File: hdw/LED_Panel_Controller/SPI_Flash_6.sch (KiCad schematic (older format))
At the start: 0 parts

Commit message: more schematic development
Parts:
- added C? (x2): 0.1uF, Capacitors_SMD:C_0603, symbol Custom_Library:C_Custom
- added D?: Green, LEDs:LED_0603, symbol Device:LED
- added R? (x4): 10k, Resistors_SMD:R_0603, symbol Custom_Library:R_Custom
- added R? (x4): 10, symbol Custom_Library:R_Custom
- added R?: 1k, Resistors_SMD:R_0603, symbol Custom_Library:R_Custom
- added U?: SST25VF080B-50-4I-S2AF, Package_SO:SOIC-8_5.275x5.275mm_P1.27mm, symbol Memory_Flash:SST25VF080B-50-4x-S2Ax
- added U?: 74LVC1G97, Package_TO_SOT_SMD:SOT-363_SC-70-6, symbol Custom_Library:74LVC1G97_Power_BUF
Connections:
- new net: R?.1, R?.1, U?.2 (SO)
- new net: R?.1, R?.1, U?.5 (SI)
- new net: D?.1 (K), U?.4
- new net: D?.2 (A), R?.2
- new net: R?.1, R?.2, U?.1 (~CE)
- new net: R?.1, R?.1, U?.6 (SCK)
- new net +3V3: C?.1, C?.1, R?.1, R?.1, U?.3 (~WP~), U?.5 (VCC), U?.7 (~HOLD~), U?.8 (VDD)
- new net FLASH_SPI_MISO: R?.2
- new net FLASH_SPI_MOSI: R?.2
- new net FLASH_SPI_SCK: R?.2
- new net GND: C?.2, C?.2, R?.2, R?.2, R?.2, U?.2 (GND), U?.3 (GND), U?.4 (VSS), U?.6 (GND)
- new net ~FLASH_SPI_CE6: R?.2, U?.1

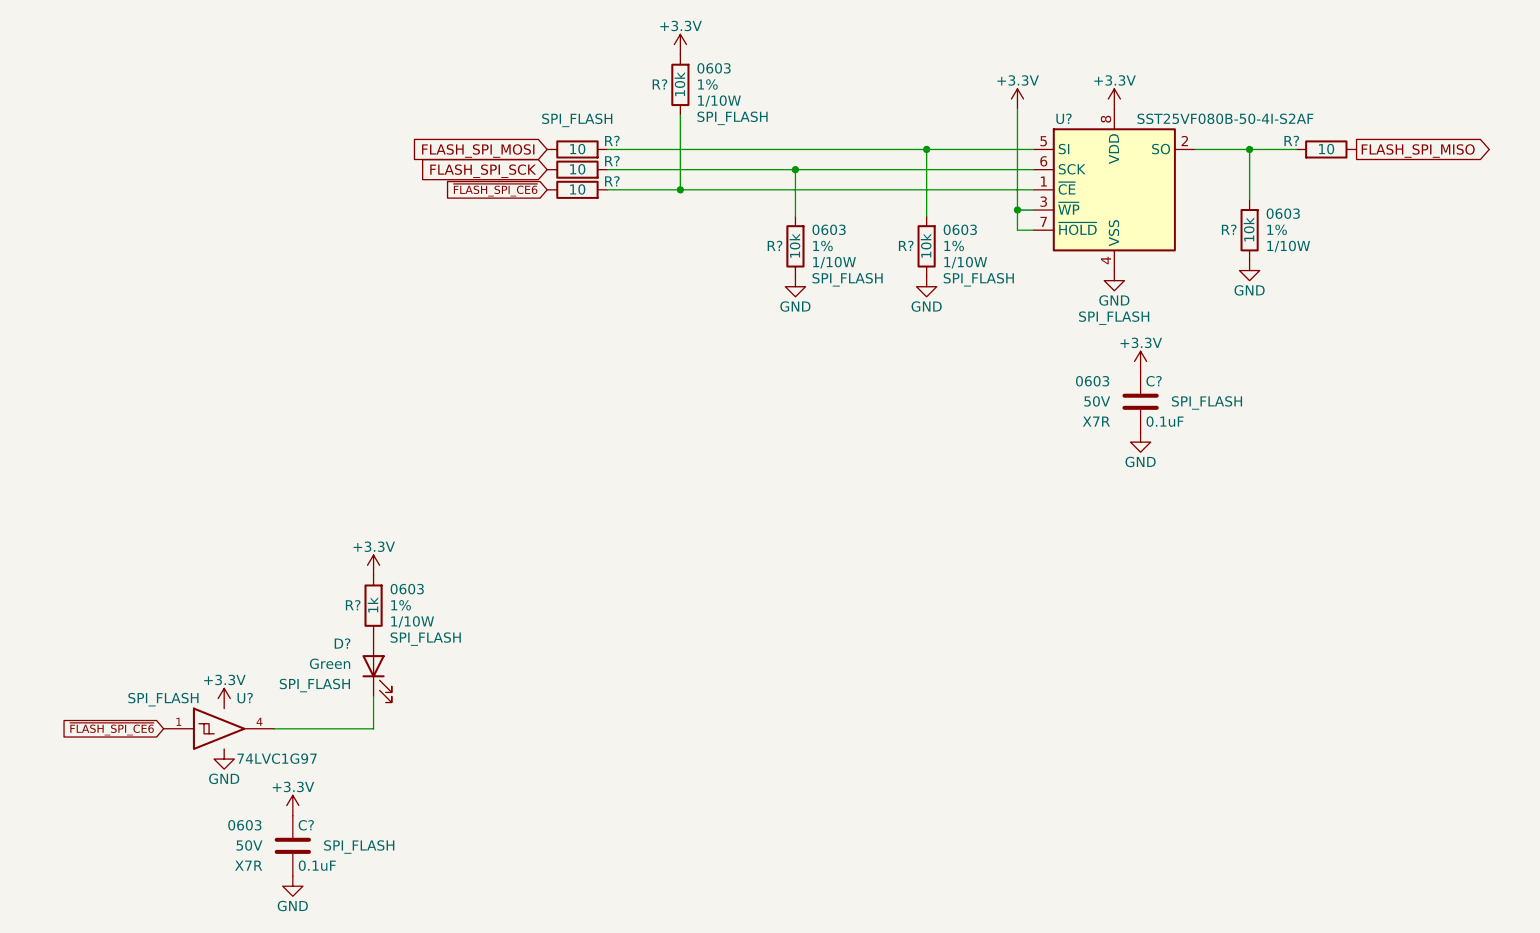
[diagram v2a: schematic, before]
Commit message: added digikey pns, footprints, bom scrubbed
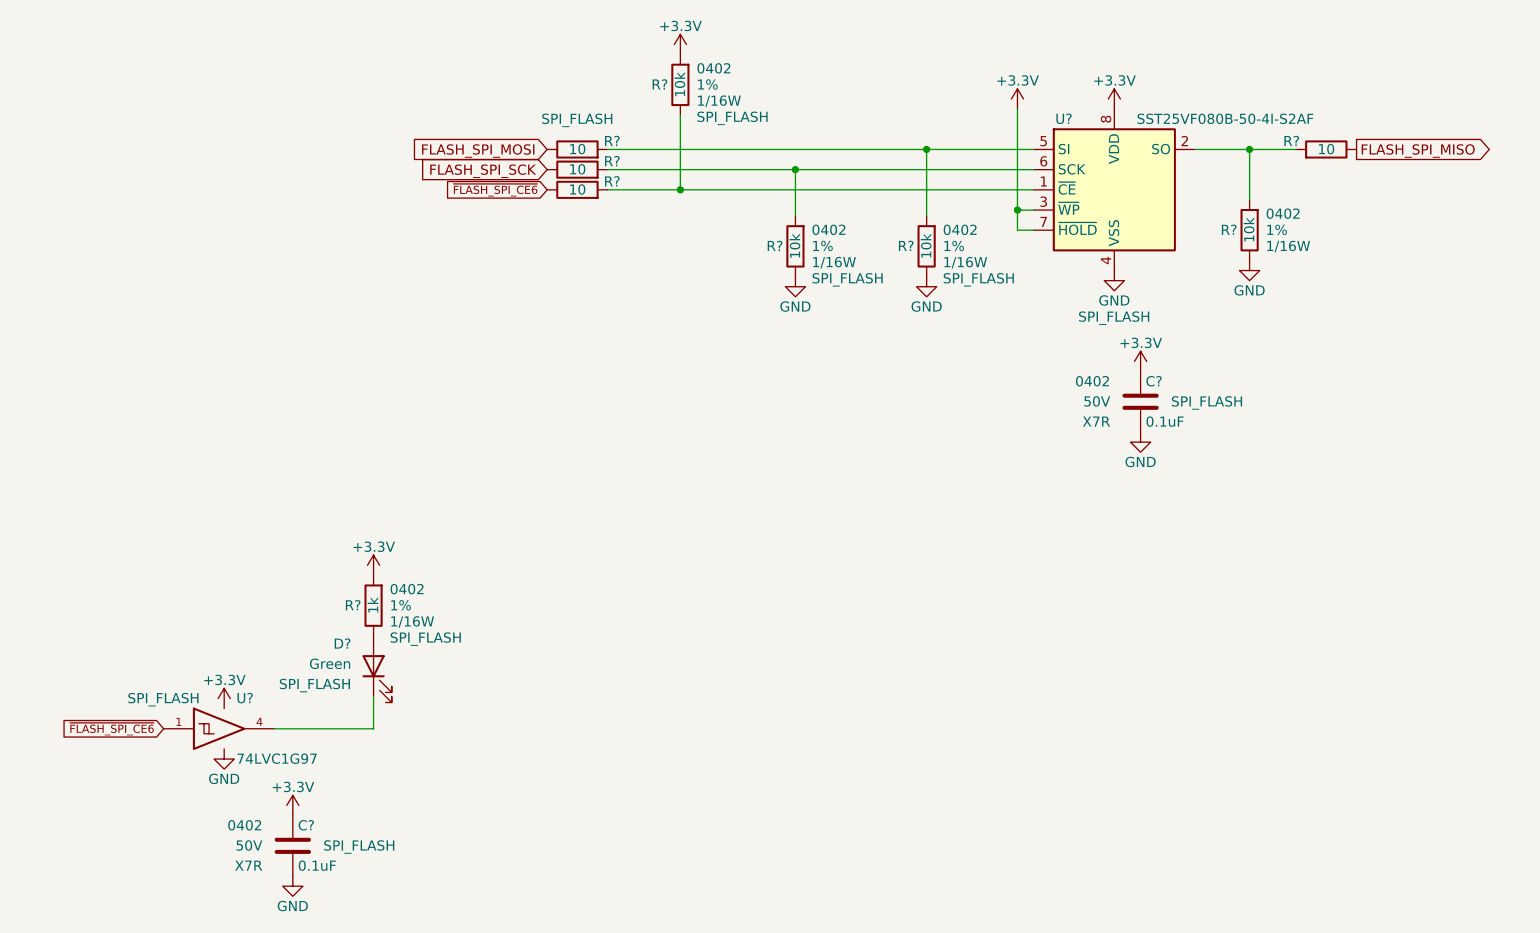
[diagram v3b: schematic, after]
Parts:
- C? (x2): footprint Capacitors_SMD:C_0603 -> Capacitors_SMD:C_0402; Digi-Key PN 311-1344-1-ND -> 490-10701-1-ND; display_footprint 0603 -> 0402
- D?: footprint LEDs:LED_0603 -> LEDs:LED_0402; Digi-Key PN 160-1446-1-ND -> 1497-1219-1-ND
- R? (x4): footprint Resistors_SMD:R_0603 -> Resistors_SMD:R_0402; Digi-Key PN RMCF0603FT10K0CT-ND -> RMCF0402FT10K0CT-ND; Wattage 1/10W -> 1/16W; display_footprint 0603 -> 0402
- R? (x4): footprint (none) -> Resistors_SMD:R_0402; Digi-Key PN (none) -> RMCF0402FT10R0CT-ND
- R?: footprint Resistors_SMD:R_0603 -> Resistors_SMD:R_0402; Digi-Key PN RMCF0603FT10K0CT-ND -> RMCF0402FT1K00CT-ND; Wattage 1/10W -> 1/16W; display_footprint 0603 -> 0402
- U?: Digi-Key PN SST25VF080B-50-4I-S2AF-TCT-ND -> SST25VF080B-50-4I-S2AE-T
- U?: Digi-Key PN (none) -> 1727-1772-1-ND
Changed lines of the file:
@@
 F 0 "R?" H 6690 3850 50  0000 R CNN
 F 1 "10k" V 6750 3850 50  0000 C CNN
-F 2 "Resistors_SMD:R_0603" H 6750 3850 50  0001 C CNN
+F 2 "Resistors_SMD:R_0402" H 6750 3850 50  0001 C CNN
 F 3 "" H 6750 3850 50  0001 C CNN
-F 4 "0603" H 6830 3930 50  0000 L CNN "display_footprint"
+F 4 "0402" H 6830 3930 50  0000 L CNN "display_footprint"
 F 5 "1%" H 6830 3850 50  0000 L CNN "Tolerance"
-F 6 "1/10W" H 6830 3770 50  0000 L CNN "Wattage"
-F 7 "RMCF0603FT10K0CT-ND" H 7050 4250 60  0001 C CNN "Digi-Key PN"
+F 6 "1/16W" H 6830 3770 50  0000 L CNN "Wattage"
+F 7 "RMCF0402FT10K0CT-ND" H 7050 4250 60  0001 C CNN "Digi-Key PN"
 	1    6750 3850
 	1    0    0    -1
@@
 F 0 "R?" V 3380 3580 50  0000 L CNN
 F 1 "10" V 3420 3450 50  0000 C CNN
-F 2 "" H 3420 3450 50  0001 C CNN
+F 2 "Resistors_SMD:R_0402" H 3420 3450 50  0001 C CNN
 F 3 "" H 3420 3450 50  0001 C CNN
 F 4 "0402" V 3520 3450 50  0001 C CNN "display_footprint"
@@
 F 6 "1/16W" V 3720 3450 50  0001 C CNN "Wattage"
 F 7 "SPI_FLASH" V 3270 3450 50  0000 C CNN "Configuration"
+F 8 "RMCF0402FT10R0CT-ND" H 3420 3450 50  0001 C CNN "Digi-Key PN"
 	1    3420 3450
 	0    1    1    0
@@
 F 0 "C?" H 2035 7000 50  0000 L CNN
 F 1 "0.1uF" H 2035 6800 50  0000 L CNN
-F 2 "Capacitors_SMD:C_0603" H 2048 6750 50  0001 C CNN
+F 2 "Capacitors_SMD:C_0402" H 2048 6750 50  0001 C CNN
 F 3 "" H 2035 7000 50  0001 C CNN
-F 4 "0603" H 1860 7000 50  0000 R CNN "display_footprint"
+F 4 "0402" H 1860 7000 50  0000 R CNN "display_footprint"
 F 5 "50V" H 1860 6900 50  0000 R CNN "Voltage"
 F 6 "X7R" H 1860 6800 50  0000 R CNN "Dielectric"
-F 7 "311-1344-1-ND" H 2435 7400 60  0001 C CNN "Digi-Key PN"
+F 7 "490-10701-1-ND" H 2435 7400 60  0001 C CNN "Digi-Key PN"
 F 8 "SPI_FLASH" H 2340 6900 50  0000 C CNN "Configuration"
 	1    2010 6900
@@
 F 0 "D?" V 2520 6120 50  0000 L CNN
 F 1 "Green" V 2420 6120 50  0000 L CNN
-F 2 "LEDs:LED_0603" H 2410 6010 50  0001 C CNN
+F 2 "LEDs:LED_0402" H 2410 6010 50  0001 C CNN
 F 3 "~" H 2410 6010 50  0001 C CNN
-F 4 "160-1446-1-ND" H -2600 3010 50  0001 C CNN "Digi-Key PN"
+F 4 "1497-1219-1-ND" H -2600 3010 50  0001 C CNN "Digi-Key PN"
 F 5 "SPI_FLASH" V 2320 6120 50  0000 L CNN "Configuration"
 	1    2410 6010
@@
 F 2 "Package_SO:SOIC-8_5.275x5.275mm_P1.27mm" H 6080 2950 50  0001 C CNN
 F 3 "http://ww1.microchip.com/downloads/en/DeviceDoc/20005045C.pdf" H 6030 4200 50  0001 C CNN
-F 4 "SST25VF080B-50-4I-S2AF-TCT-ND" H 6080 3650 50  0001 C CNN "Digi-Key PN"
+F 4 "SST25VF080B-50-4I-S2AE-T" H 6080 3650 50  0001 C CNN "Digi-Key PN"
 F 5 "SPI_FLASH" H 6080 3020 50  0000 C CNN "Configuration"
 	1    6080 3650
@@
 F 0 "R?" H 4440 3930 50  0000 R CNN
 F 1 "10k" V 4500 3930 50  0000 C CNN
-F 2 "Resistors_SMD:R_0603" H 4500 3930 50  0001 C CNN
+F 2 "Resistors_SMD:R_0402" H 4500 3930 50  0001 C CNN
 F 3 "" H 4500 3930 50  0001 C CNN
-F 4 "0603" H 4580 4010 50  0000 L CNN "display_footprint"
+F 4 "0402" H 4580 4010 50  0000 L CNN "display_footprint"
 F 5 "1%" H 4580 3930 50  0000 L CNN "Tolerance"
-F 6 "1/10W" H 4580 3850 50  0000 L CNN "Wattage"
-F 7 "RMCF0603FT10K0CT-ND" H 4800 4330 60  0001 C CNN "Digi-Key PN"
+F 6 "1/16W" H 4580 3850 50  0000 L CNN "Wattage"
+F 7 "RMCF0402FT10K0CT-ND" H 4800 4330 60  0001 C CNN "Digi-Key PN"
 F 8 "SPI_FLASH" H 4580 3770 50  0000 L CNN "Configuration"
 	1    4500 3930
@@
 F 0 "R?" V 3380 3680 50  0000 L CNN
 F 1 "10" V 3420 3550 50  0000 C CNN
-F 2 "" H 3420 3550 50  0001 C CNN
+F 2 "Resistors_SMD:R_0402" H 3420 3550 50  0001 C CNN
 F 3 "" H 3420 3550 50  0001 C CNN
 F 4 "0402" V 3520 3550 50  0001 C CNN "display_footprint"
@@
 F 6 "1/16W" V 3720 3550 50  0001 C CNN "Wattage"
 F 7 "SPI_FLASH" H 3420 3550 50  0001 C CNN "Configuration"
+F 8 "RMCF0402FT10R0CT-ND" H 3420 3550 50  0001 C CNN "Digi-Key PN"
 	1    3420 3550
 	0    1    1    0
@@
 F 0 "R?" V 3380 3780 50  0000 L CNN
 F 1 "10" V 3420 3650 50  0000 C CNN
-F 2 "" H 3420 3650 50  0001 C CNN
+F 2 "Resistors_SMD:R_0402" H 3420 3650 50  0001 C CNN
 F 3 "" H 3420 3650 50  0001 C CNN
 F 4 "0402" V 3520 3650 50  0001 C CNN "display_footprint"
@@
 F 6 "1/16W" V 3720 3650 50  0001 C CNN "Wattage"
 F 7 "SPI_FLASH" H 3420 3650 50  0001 C CNN "Configuration"
+F 8 "RMCF0402FT10R0CT-ND" H 3420 3650 50  0001 C CNN "Digi-Key PN"
 	1    3420 3650
 	0    1    1    0
@@
 F 0 "R?" V 7090 3580 50  0000 L CNN
 F 1 "10" V 7130 3450 50  0000 C CNN
-F 2 "" H 7130 3450 50  0001 C CNN
+F 2 "Resistors_SMD:R_0402" H 7130 3450 50  0001 C CNN
 F 3 "" H 7130 3450 50  0001 C CNN
 F 4 "0402" V 7230 3450 50  0001 C CNN "display_footprint"
 F 5 "1%" V 7330 3450 50  0001 C CNN "Tolerance"
 F 6 "1/16W" V 7430 3450 50  0001 C CNN "Wattage"
+F 7 "RMCF0402FT10R0CT-ND" H 7130 3450 50  0001 C CNN "Digi-Key PN"
 	1    7130 3450
 	0    -1   1    0
@@
 F 3 "http://www.ti.com/lit/ds/symlink/sn74lvc1g97.pdf" H 1720 6320 50  0001 C CNN
 F 4 "SPI_FLASH" H 1370 6470 50  0000 C CNN "Configuration"
+F 5 "1727-1772-1-ND" H 1670 6320 50  0001 C CNN "Digi-Key PN"
 	1    1670 6320
 	1    0    0    -1
@@
 F 0 "R?" H 5090 3930 50  0000 R CNN
 F 1 "10k" V 5150 3930 50  0000 C CNN
-F 2 "Resistors_SMD:R_0603" H 5150 3930 50  0001 C CNN
+F 2 "Resistors_SMD:R_0402" H 5150 3930 50  0001 C CNN
 F 3 "" H 5150 3930 50  0001 C CNN
-F 4 "0603" H 5230 4010 50  0000 L CNN "display_footprint"
+F 4 "0402" H 5230 4010 50  0000 L CNN "display_footprint"
 F 5 "1%" H 5230 3930 50  0000 L CNN "Tolerance"
-F 6 "1/10W" H 5230 3850 50  0000 L CNN "Wattage"
-F 7 "RMCF0603FT10K0CT-ND" H 5450 4330 60  0001 C CNN "Digi-Key PN"
+F 6 "1/16W" H 5230 3850 50  0000 L CNN "Wattage"
+F 7 "RMCF0402FT10K0CT-ND" H 5450 4330 60  0001 C CNN "Digi-Key PN"
 F 8 "SPI_FLASH" H 5230 3770 50  0000 L CNN "Configuration"
 	1    5150 3930
@@
 F 0 "R?" H 3870 3130 50  0000 R CNN
 F 1 "10k" V 3930 3130 50  0000 C CNN
-F 2 "Resistors_SMD:R_0603" H 3930 3130 50  0001 C CNN
+F 2 "Resistors_SMD:R_0402" H 3930 3130 50  0001 C CNN
 F 3 "" H 3930 3130 50  0001 C CNN
-F 4 "0603" H 4010 3210 50  0000 L CNN "display_footprint"
+F 4 "0402" H 4010 3210 50  0000 L CNN "display_footprint"
 F 5 "1%" H 4010 3130 50  0000 L CNN "Tolerance"
-F 6 "1/10W" H 4010 3050 50  0000 L CNN "Wattage"
-F 7 "RMCF0603FT10K0CT-ND" H 4230 3530 60  0001 C CNN "Digi-Key PN"
+F 6 "1/16W" H 4010 3050 50  0000 L CNN "Wattage"
+F 7 "RMCF0402FT10K0CT-ND" H 4230 3530 60  0001 C CNN "Digi-Key PN"
 F 8 "SPI_FLASH" H 4010 2970 50  0000 L CNN "Configuration"
 	1    3930 3130
@@
 F 0 "R?" H 2350 5710 50  0000 R CNN
 F 1 "1k" V 2410 5710 50  0000 C CNN
-F 2 "Resistors_SMD:R_0603" H 2410 5710 50  0001 C CNN
+F 2 "Resistors_SMD:R_0402" H 2410 5710 50  0001 C CNN
 F 3 "" H 2410 5710 50  0001 C CNN
-F 4 "0603" H 2490 5790 50  0000 L CNN "display_footprint"
+F 4 "0402" H 2490 5790 50  0000 L CNN "display_footprint"
 F 5 "1%" H 2490 5710 50  0000 L CNN "Tolerance"
-F 6 "1/10W" H 2490 5630 50  0000 L CNN "Wattage"
-F 7 "RMCF0603FT10K0CT-ND" H 2710 6110 60  0001 C CNN "Digi-Key PN"
+F 6 "1/16W" H 2490 5630 50  0000 L CNN "Wattage"
+F 7 "RMCF0402FT1K00CT-ND" H 2710 6110 60  0001 C CNN "Digi-Key PN"
 F 8 "SPI_FLASH" H 2490 5550 50  0000 L CNN "Configuration"
 	1    2410 5710
@@
 F 0 "C?" H 6235 4800 50  0000 L CNN
 F 1 "0.1uF" H 6235 4600 50  0000 L CNN
-F 2 "Capacitors_SMD:C_0603" H 6248 4550 50  0001 C CNN
+F 2 "Capacitors_SMD:C_0402" H 6248 4550 50  0001 C CNN
 F 3 "" H 6235 4800 50  0001 C CNN
-F 4 "0603" H 6060 4800 50  0000 R CNN "display_footprint"
+F 4 "0402" H 6060 4800 50  0000 R CNN "display_footprint"
 F 5 "50V" H 6060 4700 50  0000 R CNN "Voltage"
 F 6 "X7R" H 6060 4600 50  0000 R CNN "Dielectric"
-F 7 "311-1344-1-ND" H 6635 5200 60  0001 C CNN "Digi-Key PN"
+F 7 "490-10701-1-ND" H 6635 5200 60  0001 C CNN "Digi-Key PN"
 F 8 "SPI_FLASH" H 6540 4700 50  0000 C CNN "Configuration"
 	1    6210 4700
